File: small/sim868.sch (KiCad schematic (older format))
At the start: 28 parts, among them J1 SIM_Card, J10 Conn_01x06_Female, Q1 2N7002, U16 SRV05-4

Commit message: simcard colder changed to 78800-0001
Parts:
- removed D? (x2): LED, LED_SMD:LED_0805_2012Metric, symbol Device:LED
- removed J1: SIM_Card, symbol Connector:SIM_Card
- removed R? (x2): 100, Resistor_SMD:R_0603_1608Metric, symbol Device:R
- added J?: 78800-0001, 788000001, symbol simcard:78800-0001
- C38: footprint (none) -> Resistor_SMD:R_0805_2012Metric; LCSC (none) -> C45783; MPN (none) -> CL21A226MAQNNNE; Price (none) -> 0.0526
- C43: footprint (none) -> Capacitor_SMD:C_0603_1608Metric; LCSC (none) -> C14663
- C45: footprint (none) -> Capacitor_SMD:C_0603_1608Metric; LCSC (none) -> C1671
- C46: footprint (none) -> Capacitor_Tantalum_SMD:CP_EIA-3528-21_Kemet-B; LCSC (none) -> C16133
- D11: footprint (none) -> Diode_SMD:D_MiniMELF; LCSC (none) -> C8062; MPN (none) -> ZMM5V6
- gave numbers to parts that had none: 7
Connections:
- net labels added: POWER_SIM, SIM_CLK, SIM_IO, SIM_RST, SIM_VDD
- wire segments 79 -> 75
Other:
- moved on the sheet: R43, R44, R45

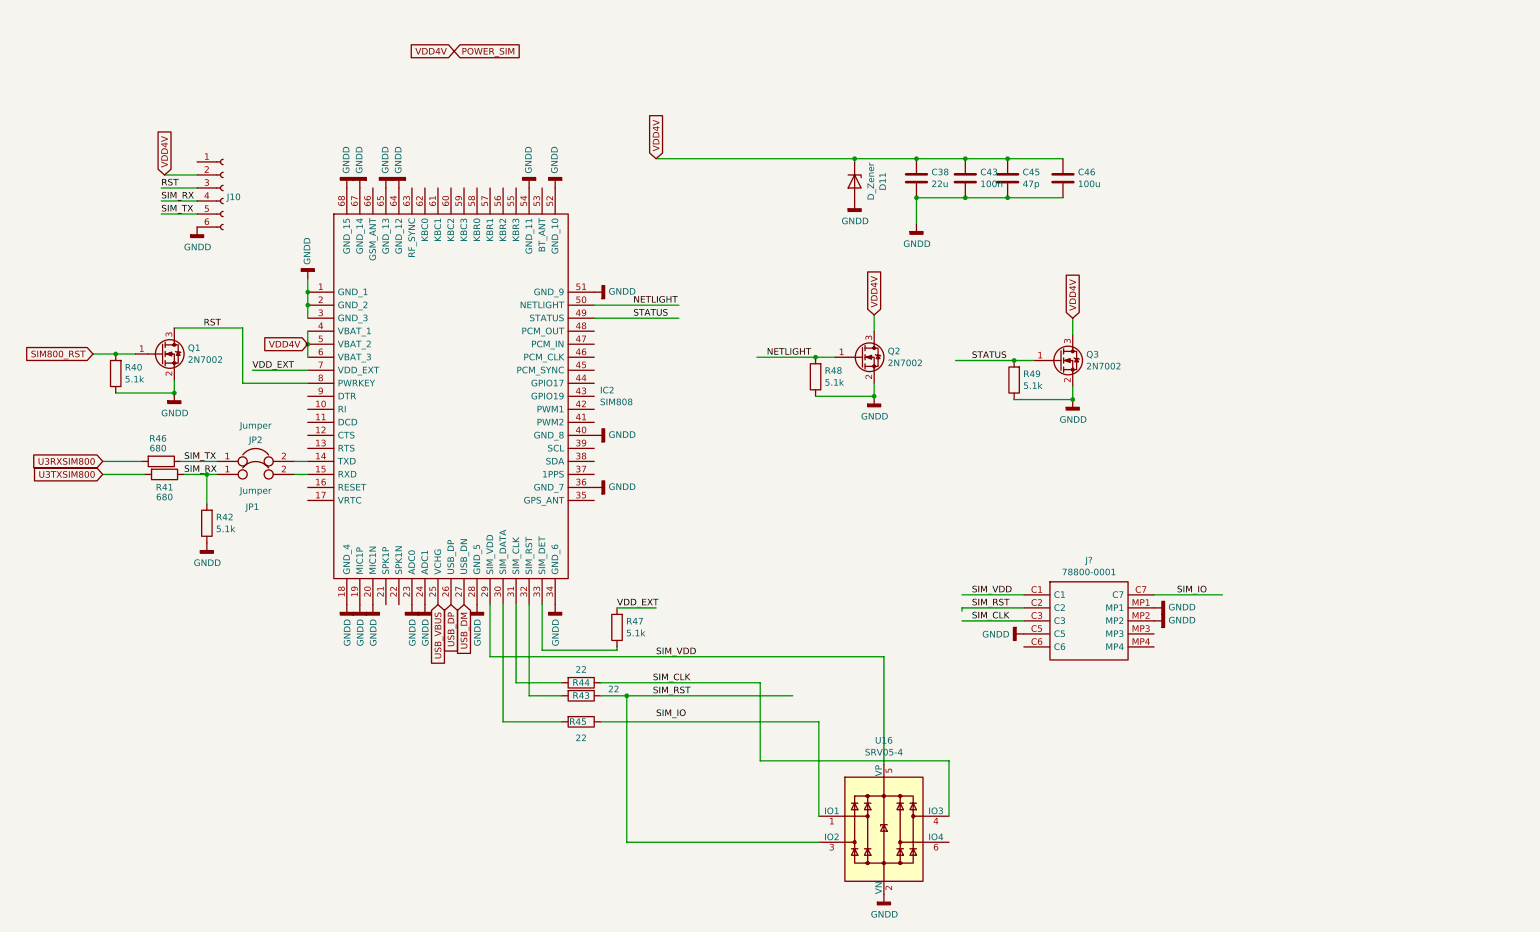
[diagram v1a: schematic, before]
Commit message: All routed PGEC1 grounded according to errata
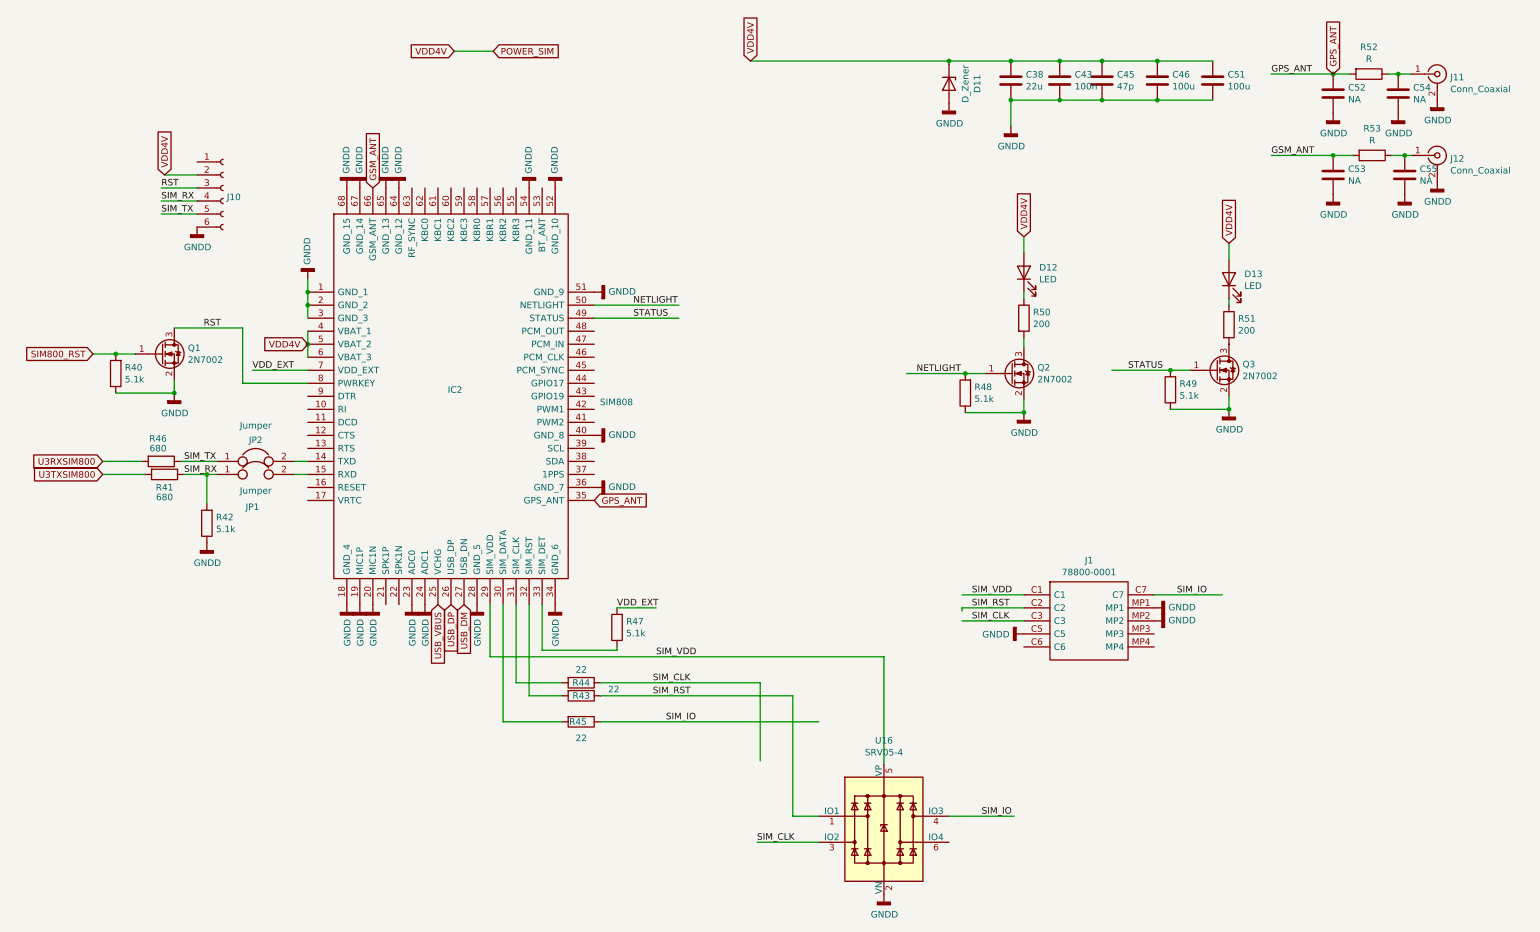
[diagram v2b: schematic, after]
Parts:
- added C51: 100u, Capacitor_Tantalum_SMD:CP_EIA-3528-21_Kemet-B, symbol Device:C
- added C52, C53, C54, C55: NA, Resistor_SMD:R_0603_1608Metric, symbol Device:C
- added D12, D13: LED, LED_SMD:LED_0805_2012Metric_Pad1.15x1.40mm_HandSolder, symbol Device:LED
- added J11, J12: Conn_Coaxial, Connector_Coaxial:SMA_Amphenol_901-144_Vertical, symbol Connector:Conn_Coaxial
- added R50, R51: 200, Resistor_SMD:R_0603_1608Metric, symbol Device:R
- added R52, R53: R, Resistor_SMD:R_0603_1608Metric, symbol Device:R
- gave numbers to parts that had none: 1
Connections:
- net labels added: GPS_ANT, GSM_ANT
- wire segments 75 -> 87
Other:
- moved on the sheet: C38, C43, C45, C46, D11, Q2, Q3, R48, R49

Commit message: GPS connector moved,
antenna matching networks removed

SUPERCAPACITOR from jlpcb used.
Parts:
- removed C52, C53, C54, C55: NA, Resistor_SMD:R_0603_1608Metric, symbol Device:C
- removed R52, R53: R, Resistor_SMD:R_0603_1608Metric, symbol Device:R
- added L3: INDUCTOR, Inductor_SMD:L_0603_1608Metric, symbol pspice:INDUCTOR
- added R55: R, Resistor_SMD:R_0603_1608Metric, symbol Device:R
- J11, J12: Website (none) -> mouser; source mouser -> (none)
- R41, R46: value 680 -> 1k; LCSC C23228 -> C21190
- U16: LCSC (none) -> C85364
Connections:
- wire segments 87 -> 83
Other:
- moved on the sheet: R41
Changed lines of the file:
@@
 Wire Wire Line
 	250  3875 550  3875
-$Comp
-L Device:R R46
-U 1 1 603ACA9E
-P 700 3875
-F 0 "R46" V 525 3850 50  0000 C CNN
-F 1 "680" V 600 3850 50  0000 C CNN
-F 2 "Resistor_SMD:R_0603_1608Metric" V 630 3875 50  0001 C CNN
-F 3 "~" H 700 3875 50  0001 C CNN
-F 4 "C23228" V 700 3875 50  0001 C CNN "LCSC"
-	1    700  3875
-	0    1    1    0
-$EndComp
 Wire Wire Line
 	3425 4975 3425 5575
-Wire Wire Line
-	5300 5575 5300 6175
 Wire Wire Line
 	3525 4975 3525 5675
@@
 Wire Wire Line
 	1125 3975 1050 3975
-Wire Wire Line
-	1050 3975 875  3975
 Connection ~ 1050 3975
-Wire Wire Line
-	575  3975 250  3975
-$Comp
-L Device:R R41
-U 1 1 602571F5
-P 725 3975
-F 0 "R41" V 825 3975 50  0000 C CNN
-F 1 "680" V 900 3975 50  0000 C CNN
-F 2 "Resistor_SMD:R_0603_1608Metric" V 655 3975 50  0001 C CNN
-F 3 "~" H 725 3975 50  0001 C CNN
-F 4 "C23228" V 725 3975 50  0001 C CNN "LCSC"
-	1    725  3975
-	0    1    1    0
-$EndComp
 Connection ~ 6750 800
 Wire Wire Line
@@
 Wire Wire Line
 	3525 5675 3775 5675
-Wire Wire Line
-	4075 5575 5300 5575
 $Comp
 L Connector:Conn_Coaxial J11
@@
 F 4 "73391-0070" H 10500 900 50  0001 C CNN "MPN"
 F 5 "NA" H 10500 900 50  0001 C CNN "LCSC"
-F 6 "mouser" H 10500 900 50  0001 C CNN "source"
+F 6 "" H 10500 900 50  0001 C CNN "source"
+F 7 "mouser" H 10500 900 50  0001 C CNN "Website"
 	1    10500 900
 	1    0    0    -1
@@
 Text GLabel 2325 1775 1    50   Input ~ 0
 GSM_ANT
-Text GLabel 4025 4175 2    50   Input ~ 0
+Text GLabel 4700 4175 2    50   Input ~ 0
 GPS_ANT
-$Comp
-L Device:R R52
-U 1 1 605199D1
-P 9975 900
-F 0 "R52" V 9768 900 50  0000 C CNN
-F 1 "R" V 9859 900 50  0000 C CNN
-F 2 "Resistor_SMD:R_0603_1608Metric" V 9905 900 50  0001 C CNN
-F 3 "~" H 9975 900 50  0001 C CNN
-	1    9975 900
-	0    1    1    0
-$EndComp
-Wire Wire Line
-	10300 900  10200 900
-Text Label 9225 900  0    50   ~ 0
+Text Label 9525 900  0    50   ~ 0
 GPS_ANT
 Text Label 9225 1525 0    50   ~ 0
 GSM_ANT
-$Comp
-L Device:R R53
-U 1 1 605220BC
-P 10000 1525
-F 0 "R53" V 9793 1525 50  0000 C CNN
-F 1 "R" V 9884 1525 50  0000 C CNN
-F 2 "Resistor_SMD:R_0603_1608Metric" V 9930 1525 50  0001 C CNN
-F 3 "~" H 10000 1525 50  0001 C CNN
-	1    10000 1525
-	0    1    1    0
-$EndComp
-$Comp
-L Device:C C54
-U 1 1 60526717
-P 10200 1050
-F 0 "C54" H 10315 1096 50  0000 L CNN
-F 1 "NA" H 10315 1005 50  0000 L CNN
-F 2 "Resistor_SMD:R_0603_1608Metric" H 10238 900 50  0001 C CNN
-F 3 "~" H 10200 1050 50  0001 C CNN
-	1    10200 1050
-	1    0    0    -1
-$EndComp
-Connection ~ 10200 900
-Wire Wire Line
-	10200 900  10125 900
-$Comp
-L power:GNDD #PWR0169
-U 1 1 605272B2
-P 10200 1200
-F 0 "#PWR0169" H 10200 950 50  0001 C CNN
-F 1 "GNDD" H 10204 1045 50  0000 C CNN
-F 2 "" H 10200 1200 50  0001 C CNN
-F 3 "" H 10200 1200 50  0001 C CNN
-	1    10200 1200
-	1    0    0    -1
-$EndComp
-$Comp
-L Device:C C52
-U 1 1 60528191
-P 9700 1050
-F 0 "C52" H 9815 1096 50  0000 L CNN
-F 1 "NA" H 9815 1005 50  0000 L CNN
-F 2 "Resistor_SMD:R_0603_1608Metric" H 9738 900 50  0001 C CNN
-F 3 "~" H 9700 1050 50  0001 C CNN
-	1    9700 1050
-	1    0    0    -1
-$EndComp
-$Comp
-L power:GNDD #PWR0177
-U 1 1 60528197
-P 9700 1200
-F 0 "#PWR0177" H 9700 950 50  0001 C CNN
-F 1 "GNDD" H 9704 1045 50  0000 C CNN
-F 2 "" H 9700 1200 50  0001 C CNN
-F 3 "" H 9700 1200 50  0001 C CNN
-	1    9700 1200
-	1    0    0    -1
-$EndComp
-Connection ~ 9700 900
-Wire Wire Line
-	9700 900  9825 900
-$Comp
-L Device:C C55
-U 1 1 6052CA7C
-P 10250 1675
-F 0 "C55" H 10365 1721 50  0000 L CNN
-F 1 "NA" H 10365 1630 50  0000 L CNN
-F 2 "Resistor_SMD:R_0603_1608Metric" H 10288 1525 50  0001 C CNN
-F 3 "~" H 10250 1675 50  0001 C CNN
-	1    10250 1675
-	1    0    0    -1
-$EndComp
-$Comp
-L power:GNDD #PWR0182
-U 1 1 6052CA82
-P 10250 1825
-F 0 "#PWR0182" H 10250 1575 50  0001 C CNN
-F 1 "GNDD" H 10254 1670 50  0000 C CNN
-F 2 "" H 10250 1825 50  0001 C CNN
-F 3 "" H 10250 1825 50  0001 C CNN
-	1    10250 1825
-	1    0    0    -1
-$EndComp
-$Comp
-L Device:C C53
-U 1 1 6052EAC0
-P 9700 1675
-F 0 "C53" H 9815 1721 50  0000 L CNN
-F 1 "NA" H 9815 1630 50  0000 L CNN
-F 2 "Resistor_SMD:R_0603_1608Metric" H 9738 1525 50  0001 C CNN
-F 3 "~" H 9700 1675 50  0001 C CNN
-	1    9700 1675
-	1    0    0    -1
-$EndComp
-$Comp
-L power:GNDD #PWR0183
-U 1 1 6052EAC6
-P 9700 1825
-F 0 "#PWR0183" H 9700 1575 50  0001 C CNN
-F 1 "GNDD" H 9704 1670 50  0000 C CNN
-F 2 "" H 9700 1825 50  0001 C CNN
-F 3 "" H 9700 1825 50  0001 C CNN
-	1    9700 1825
-	1    0    0    -1
-$EndComp
-Connection ~ 10250 1525
-Wire Wire Line
-	10250 1525 10300 1525
-Wire Wire Line
-	9225 1525 9700 1525
-Wire Wire Line
-	9225 900  9700 900
 Wire Wire Line
 	8775 1100 8350 1100
@@
 F 4 "73391-0070" H 10500 1525 50  0001 C CNN "MPN"
 F 5 "NA" H 10500 1525 50  0001 C CNN "LCSC"
-F 6 "mouser" H 10500 1525 50  0001 C CNN "source"
+F 6 "" H 10500 1525 50  0001 C CNN "source"
+F 7 "mouser" H 10500 1525 50  0001 C CNN "Website"
 	1    10500 1525
 	1    0    0    -1
 $EndComp
-Connection ~ 9700 1525
-Wire Wire Line
-	9700 1525 9850 1525
-Wire Wire Line
-	10150 1525 10250 1525
-Text GLabel 9700 900  1    50   Input ~ 0
+Text GLabel 10000 900  1    50   Input ~ 0
 GPS_ANT
 Text Label 7000 6600 0    50   ~ 0
 SIM_IO
-Wire Wire Line
-	4075 5675 5550 5675
 Wire Wire Line
 	6750 6600 7250 6600
@@
 F 2 "Package_TO_SOT_SMD:SOT-23-6" H 6950 6250 50  0001 C CNN
 F 3 "http://www.onsemi.com/pub/Collateral/SRV05-4-D.PDF" H 6250 6700 50  0001 C CNN
+F 4 "C85364" H 6250 6700 50  0001 C CNN "LCSC"
 	1    6250 6700
 	1    0    0    -1
@@
 SIM_CLK
 Wire Wire Line
-	5550 5675 5550 6600
-Wire Wire Line
-	5550 6600 5750 6600
-Wire Wire Line
 	2950 725  3250 725
+Wire Wire Line
+	4025 4175 4575 4175
+$Comp
+L pspice:INDUCTOR L3
+U 1 1 60382DDD
+P 4575 3925
+F 0 "L3" V 4529 4003 50  0000 L CNN
+F 1 "INDUCTOR" V 4620 4003 50  0000 L CNN
+F 2 "Inductor_SMD:L_0603_1608Metric" H 4575 3925 50  0001 C CNN
+F 3 "https://datasheet.lcsc.com/szlcsc/Sunlord-SDCL1608C27NJTDF_C12100.pdf" H 4575 3925 50  0001 C CNN
+F 4 "C12100" V 4575 3925 50  0001 C CNN "LCSC"
+F 5 "SDCL1608C27NJTDF" V 4575 3925 50  0001 C CNN "MPN"
+F 6 "0.0119" V 4575 3925 50  0001 C CNN "Price"
+	1    4575 3925
+	0    1    1    0
+$EndComp
+Connection ~ 4575 4175
+Wire Wire Line
+	4575 4175 4700 4175
+$Comp
+L Device:R R55
+U 1 1 603845A9
+P 4575 3450
+F 0 "R55" H 4645 3496 50  0000 L CNN
+F 1 "R" H 4645 3405 50  0000 L CNN
+F 2 "Resistor_SMD:R_0603_1608Metric" V 4505 3450 50  0001 C CNN
+F 3 "https://datasheet.lcsc.com/szlcsc/Uniroyal-Elec-0603WAF5100T5E_C23193.pdf" H 4575 3450 50  0001 C CNN
+F 4 "C23193" H 4575 3450 50  0001 C CNN "LCSC"
+F 5 "0603WAF5100T5E" H 4575 3450 50  0001 C CNN "MPN"
+F 6 "0.0019" H 4575 3450 50  0001 C CNN "Price"
+	1    4575 3450
+	1    0    0    -1
+$EndComp
+Wire Wire Line
+	4575 3600 4575 3675
+Wire Wire Line
+	4575 3300 5075 3300
+Text Label 4725 3300 0    50   ~ 0
+VDD_EXT
+Wire Wire Line
+	5275 6600 5750 6600
+Text Label 5275 6600 0    50   ~ 0
+SIM_RST
+Wire Wire Line
+	4075 5575 5750 5575
+Wire Wire Line
+	4075 5675 5750 5675
+$Comp
+L Device:R R41
+U 1 1 602571F5
+P 700 3975
+F 0 "R41" V 800 3975 50  0000 C CNN
+F 1 "1k" V 875 3975 50  0000 C CNN
+F 2 "Resistor_SMD:R_0603_1608Metric" V 630 3975 50  0001 C CNN
+F 3 "~" H 700 3975 50  0001 C CNN
+F 4 " C21190" V 700 3975 50  0001 C CNN "LCSC"
+	1    700  3975
+	0    1    1    0
+$EndComp
+$Comp
+L Device:R R46
+U 1 1 603ACA9E
+P 700 3875
+F 0 "R46" V 525 3850 50  0000 C CNN
+F 1 "1k" V 600 3850 50  0000 C CNN
+F 2 "Resistor_SMD:R_0603_1608Metric" V 630 3875 50  0001 C CNN
+F 3 "~" H 700 3875 50  0001 C CNN
+F 4 " C21190" V 700 3875 50  0001 C CNN "LCSC"
+	1    700  3875
+	0    1    1    0
+$EndComp
+Wire Wire Line
+	550  3975 250  3975
+Wire Wire Line
+	850  3975 1050 3975
+Wire Wire Line
+	9075 1525 10300 1525
+Wire Wire Line
+	9525 900  10300 900
 $EndSCHEMATC
